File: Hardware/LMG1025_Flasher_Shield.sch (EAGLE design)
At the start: 43 parts, among them K1 TLP3475R(TP,F, K2 TLP3475R(TP,F, K3 TLP3475R(TP,F, K4 TLP3475R(TP,F, U1 DS1023-25, U2 LMG1025, U3 MAX-M8, U4 74AHCT1G125DBV

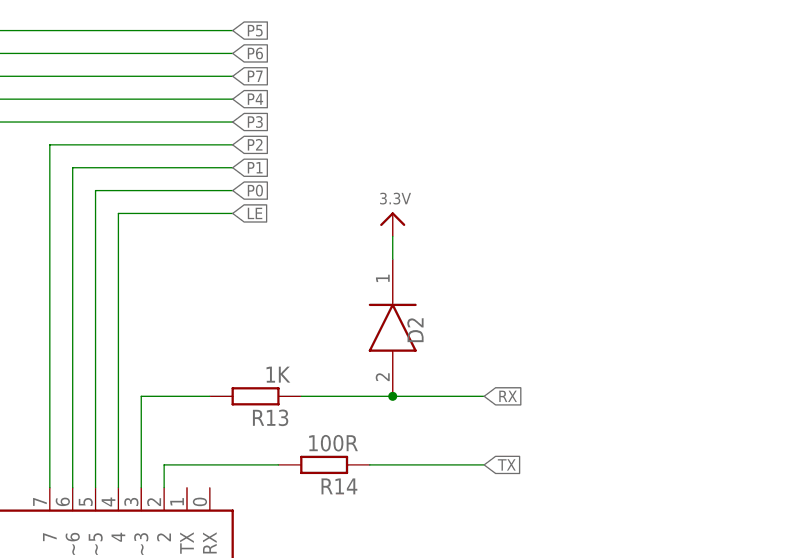
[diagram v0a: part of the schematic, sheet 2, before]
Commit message: Added the BOM
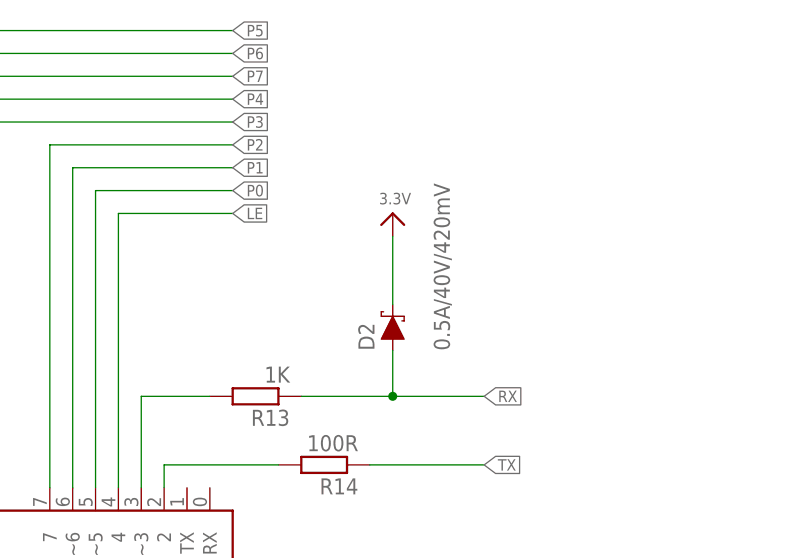
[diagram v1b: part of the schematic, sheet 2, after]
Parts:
- D2: value CD0603-B00340 -> 0.5A/40V/420mV; device SamacSys_Parts:CD0603-B00340 -> SparkFun-DiscreteSemi:DIODE-SCHOTTKY-PMEG4005EJ
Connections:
- net 3.3V: now also D2.C; no longer D2.K
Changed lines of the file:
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@@
 <?xml version="1.0" encoding="utf-8"?>
 <!DOCTYPE eagle SYSTEM "eagle.dtd">
-<eagle version="9.5.2">
+<eagle version="9.6.0">
 <drawing>
 <settings>
@@
 <part name="R12" library="resistor" library_urn="urn:adsk.eagle:library:348" deviceset="R-EU_" device="R0603" package3d_urn="urn:adsk.eagle:package:26057/1" value="10K"/>
 <part name="GND35" library="supply1" deviceset="GND" device=""/>
-<part name="D2" library="SamacSys_Parts" deviceset="CD0603-B00340" device=""/>
 <part name="U$5" library="microbuilder" deviceset="GND" device=""/>
 <part name="U3" library="ubloxLib" deviceset="MAX-M8" device=""/>
@@
 <part name="TP2" library="SparkFun-Connectors" deviceset="TEST-POINT" device="POGO_PTH"/>
 <part name="TP3" library="SparkFun-Connectors" deviceset="TEST-POINT" device="POGO_PTH"/>
+<part name="D2" library="SparkFun-DiscreteSemi" deviceset="DIODE-SCHOTTKY" device="-PMEG4005EJ" value="0.5A/40V/420mV"/>
 </parts>
 <sheets>
@@
 <attribute name="VALUE" x="248.92" y="152.4" size="1.778" layer="96"/>
 </instance>
-<instance part="D2" gate="G$1" x="152.4" y="208.28" smashed="yes" rot="R270">
-<attribute name="NAME" x="154.94" y="201.93" size="1.778" layer="95" rot="R270" align="center-left"/>
-</instance>
 <instance part="U$5" gate="G$1" x="99.06" y="40.64" smashed="yes">
 <attribute name="VALUE" x="97.536" y="38.1" size="1.27" layer="96"/>
@@
 <instance part="SUPPLY1" gate="G$1" x="228.6" y="88.9" smashed="yes">
 <attribute name="VALUE" x="228.6" y="91.694" size="1.778" layer="96" align="bottom-center"/>
+</instance>
+<instance part="D2" gate="G$1" x="152.4" y="200.66" smashed="yes" rot="R90">
+<attribute name="NAME" x="150.368" y="198.12" size="1.778" layer="95" font="vector" rot="R90"/>
+<attribute name="VALUE" x="156.972" y="198.12" size="1.778" layer="96" font="vector" rot="R90" align="top-left"/>
 </instance>
 </instances>
@@
 </segment>
 <segment>
-<pinref part="D2" gate="G$1" pin="K"/>
 <pinref part="U$4" gate="G$1" pin="3.3V"/>
-<wire x1="152.4" y1="208.28" x2="152.4" y2="210.82" width="0.1524" layer="91"/>
+<pinref part="D2" gate="G$1" pin="C"/>
+<wire x1="152.4" y1="203.2" x2="152.4" y2="210.82" width="0.1524" layer="91"/>
 </segment>
 <segment>
@@
 <wire x1="142.24" y1="193.04" x2="152.4" y2="193.04" width="0.1524" layer="91"/>
 <label x="162.56" y="193.04" size="1.27" layer="95" xref="yes"/>
-<pinref part="D2" gate="G$1" pin="A"/>
 <wire x1="152.4" y1="193.04" x2="162.56" y2="193.04" width="0.1524" layer="91"/>
 <junction x="152.4" y="193.04"/>
-</segment>
-<segment>
+<pinref part="D2" gate="G$1" pin="A"/>
+<wire x1="152.4" y1="198.12" x2="152.4" y2="193.04" width="0.1524" layer="91"/>
+</segment>
+<segment>
